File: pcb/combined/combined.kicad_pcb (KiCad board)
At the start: 2 copper layers, 113.5 x 87.5 mm, 67 parts, among them J1 5V POWER, J10 PRESSURE, J11 XIAO D0-D6, J12 XIAO D7-5V, J2 MAINS_IN, J3 VALVE, J4 PUMP, J5 CAN BUS, J6 FLOW HALL, J8 BOILER SSR, Q1 SS8050, Q2 BT136S, Q3 SS8050, Q4 BT136S, Q5 AO3401A, Q6 2N7002, U1 MOC3043M, U2 MOC3023M, U3 EL817C, U4 TJA1051T/3, U5 TMP102AIDRLR, U6 ADS1115IDGSR

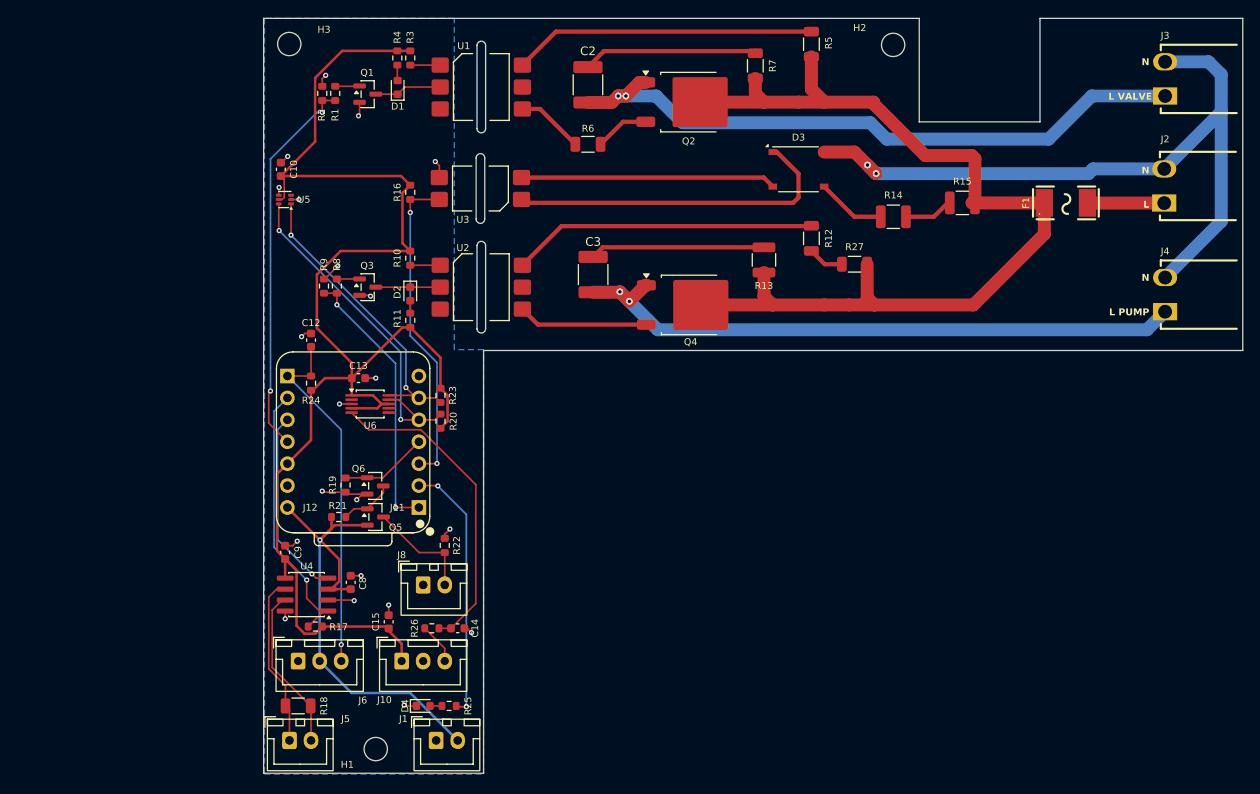
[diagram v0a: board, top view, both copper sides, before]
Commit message: Draw the combined v2 schematic: 24 V buck and isolated gear pump interface
The pump dimmer and the zero-cross detector leave the board; the 230 V
valve channel stays. J7 brings 24 V from the pump supply to an
LMR33630A buck (5.02 V, enable at 18.4 V, off at 16.9 V), and J1 now sends
5 V to the screen. Two EL817C keep the pump's signal wires on their
isolated side: U8 turns the 1 kHz PWM on GPIO1 into a filtered setpoint
from the pump's own 5 V, U9 brings the tachometer back to GPIO3. DIM and
ZC become PUMP_SPEED and PUMP_TACHO.

The XIAO 5V pin is its USB VBUS with no diode; no diode is added either,
so USB is never plugged in with the XIAO on the board. New parts take new
references, so that no low-voltage net inherits a stale Mains netclass
pattern; those patterns and the pump and zero-cross DRC rules are gone.

F1 drops to 0.5 A, now that it protects the valve alone, and the AC
tracks to 1 mm. J3 is reversed so that its N faces N on J2. The HT396R
outline follows the Kefa drawing, and J8 becomes an HT396V header whose
screw plug takes the 0.75 mm² wires to the boiler SSR.

The board has been updated from the schematic; placement and routing are
still in progress.

Co-Authored-By: Claude Opus 5.5 <noreply@anthropic.com>
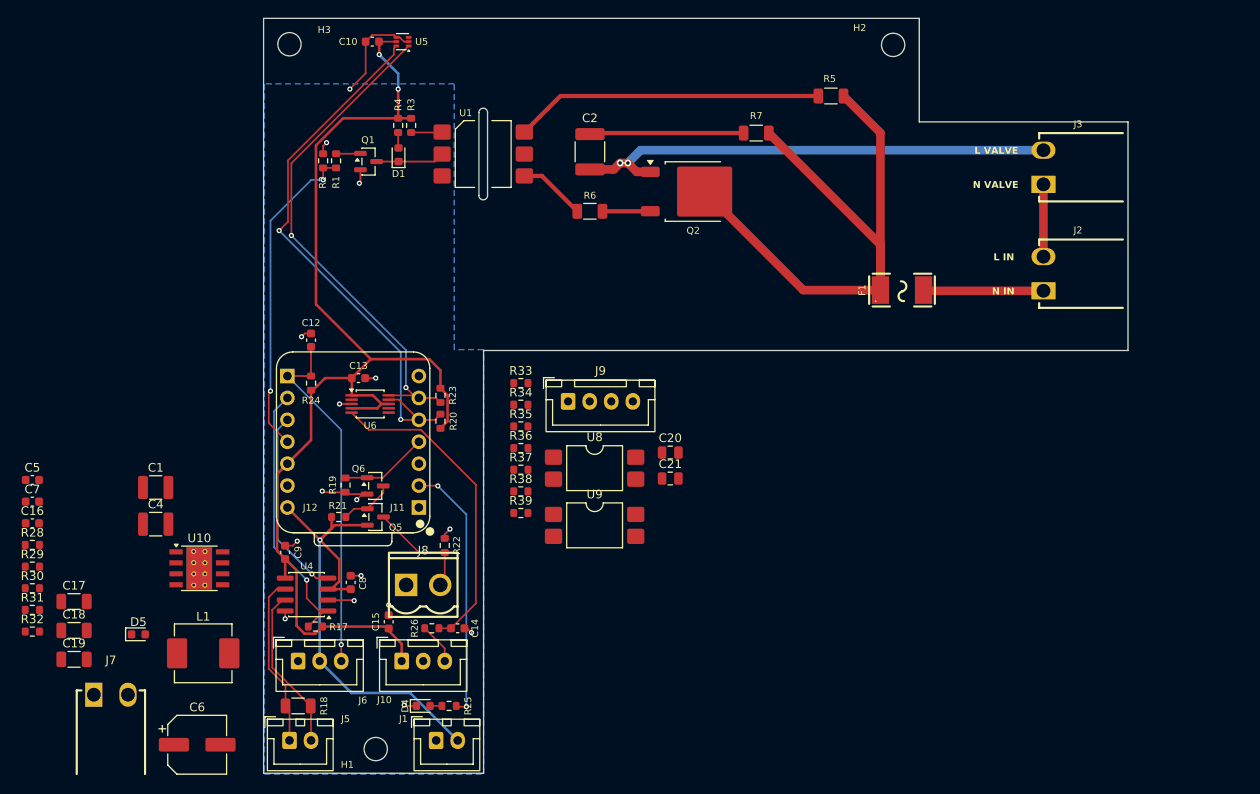
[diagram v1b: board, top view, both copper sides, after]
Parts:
- removed C3: 10nF 1kV, Capacitor_SMD:C_1812_4532Metric
- removed D2: RED, LED_SMD:LED_0603_1608Metric
- removed D3: ABS6, Diode_SMD:Diode_Bridge_Diotec_ABS
- removed J4: PUMP, Combined_Local:CONN-TH_P3.96_HT396R-3.96-2P
- removed Q3: SS8050, Package_TO_SOT_SMD:SOT-23
- removed Q4: BT136S, Package_TO_SOT_SMD:TO-252-2
- removed R10: 180, Resistor_SMD:R_0603_1608Metric
- removed R11, R8: 1k, Resistor_SMD:R_0603_1608Metric
- removed R12, R27: 510, Resistor_SMD:R_1206_3216Metric
- removed R13: 39, Resistor_SMD:R_1210_3225Metric
- removed R14, R15: 120k, Resistor_SMD:R_1210_3225Metric
- removed R16: 10k, Resistor_SMD:R_0603_1608Metric
- removed R9: 4.7k, Resistor_SMD:R_0603_1608Metric
- removed U2: MOC3023M, Combined_Local:SMDIP-6_W9.53mm_Slot
- removed U3: EL817C, Combined_Local:SMDIP-4_W9.53mm_Slot
- added C1: 10uF 50V, Capacitor_SMD:C_1210_3225Metric, F.Cu at (68.0, 101.4)
- added C16: 1uF, Capacitor_SMD:C_0603_1608Metric, F.Cu at (53.7, 105.5)
- added C17: 22uF, Capacitor_SMD:C_1206_3216Metric, F.Cu at (58.5, 114.6)
- added C18: 22uF, Capacitor_SMD:C_1206_3216Metric, F.Cu at (58.5, 118.0)
- added C19: 22uF, Capacitor_SMD:C_1206_3216Metric, F.Cu at (58.5, 121.3)
- added C20: 1.5uF, Capacitor_SMD:C_0805_2012Metric, F.Cu at (127.6, 97.3)
- added C21: 1.5uF, Capacitor_SMD:C_0805_2012Metric, F.Cu at (127.6, 100.3)
- added C4: 10uF 50V, Capacitor_SMD:C_1210_3225Metric, F.Cu at (68.0, 105.6)
- added C5: 100nF, Capacitor_SMD:C_0603_1608Metric, F.Cu at (53.7, 100.5)
- added C6: 47uF 50V, Capacitor_SMD:CP_Elec_6.3x7.7, F.Cu at (72.8, 131.2)
- added C7: 100nF, Capacitor_SMD:C_0603_1608Metric, F.Cu at (53.7, 103.0)
- added D5: 5V, LED_SMD:LED_0603_1608Metric, F.Cu at (66.0, 118.4)
- added J7: 24V IN, Combined_Local:CONN-TH_P3.96_HT396R-3.96-2P, F.Cu at (62.8, 125.4)
- added J9: PUMP, Connector_JST:JST_XH_B4B-XH-A_1x04_P2.50mm_Vertical, F.Cu at (115.8, 91.4)
- added L1: 10uH, Inductor_SMD:L_Changjiang_FXL0630, F.Cu at (73.5, 120.6)
- added R28: 100k, Resistor_SMD:R_0603_1608Metric, F.Cu at (53.7, 108.0)
- added R29: 24.9k, Resistor_SMD:R_0603_1608Metric, F.Cu at (53.7, 110.5)
- added R30: 100k, Resistor_SMD:R_0603_1608Metric, F.Cu at (53.7, 113.1)
- added R31: 7.15k, Resistor_SMD:R_0603_1608Metric, F.Cu at (53.7, 115.6)
- added R32: 1k, Resistor_SMD:R_0603_1608Metric, F.Cu at (53.7, 118.1)
- added R33: 330, Resistor_SMD:R_0603_1608Metric, F.Cu at (110.3, 89.3)
- added R34: 100k, Resistor_SMD:R_0603_1608Metric, F.Cu at (110.3, 91.8)
- added R35: 10k, Resistor_SMD:R_0603_1608Metric, F.Cu at (110.3, 94.3)
- added R36: 2.2k, Resistor_SMD:R_0603_1608Metric, F.Cu at (110.3, 96.8)
- added R37: 2.2k, Resistor_SMD:R_0603_1608Metric, F.Cu at (110.3, 99.3)
- added R38: 1.8k, Resistor_SMD:R_0603_1608Metric, F.Cu at (110.3, 101.8)
- added R39: 4.7k, Resistor_SMD:R_0603_1608Metric, F.Cu at (110.3, 104.3)
- added U10: LMR33630ADDAR, Package_SO:Texas_HSOP-8-1EP_3.9x4.9mm_P1.27mm_ThermalVias, F.Cu at (73.0, 110.8)
- added U8: EL817C, Package_DIP:SMDIP-4_W9.53mm, F.Cu at (118.9, 99.1)
- added U9: EL817C, Package_DIP:SMDIP-4_W9.53mm, F.Cu at (118.9, 105.8)
- F1: value 2A 250V fast -> 0.5A 250V fast
- J1: value 5V POWER -> 5V SCREEN
- J8: footprint Connector_JST:JST_XH_B2B-XH-A_1x02_P2.50mm_Vertical -> Combined_Local:CONN-TH_P3.96_HT396V-3.96-2P
- moved U5 22.8 mm to (96.6, 49.7)
- moved F1 21.5 mm to (154.5, 78.5)
- moved C10 18.2 mm to (93.1, 49.7), turned to 180 degrees
- moved J3 17.4 mm to (170.9, 64.3)
- moved J2 17.3 mm to (170.9, 76.6)
- moved Q2 10.4 mm to (130.4, 67.1)
- moved R1 7.81 mm to (88.9, 63.5)
- moved R2 7.81 mm to (87.4, 63.5)
- moved D1 7.81 mm to (96.1, 62.8)
- moved Q1 7.81 mm to (92.7, 63.6)
- moved R3 7.81 mm to (97.6, 59.4)
- moved R4 7.81 mm to (96.1, 59.4)
- moved R7 7.80 mm to (137.6, 60.3), turned to 180 degrees
- moved C2 7.77 mm to (118.3, 62.5)
- moved U1 7.77 mm to (106.0, 62.7)
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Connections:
- J11 pad 1: DIM -> PUMP_SPEED
- J11 pad 3: ZC -> PUMP_TACHO
- J3 pad 1: /L_VALVE -> /N
- J3 pad 2: /N -> /L_VALVE
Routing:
- net /N: track 84.8 -> 8.38 mm, vias 2 -> 0
- net /L_PUMP: track 73.3 -> 0.00 mm, vias 2 -> 0
- net /L: track 113.3 -> 72.7 mm
- net Net-(D3-+): track 40.0 -> 0.00 mm
- net ZC: track 37.4 -> 0.00 mm, vias 2 -> 0
- net Net-(R12-Pad1): track 35.4 -> 0.00 mm
- net DIM: track 31.9 -> 0.00 mm, vias 2 -> 0
- net +3V3: track 165.1 -> 134.4 mm, vias 0 -> 2
- net Net-(D3--): track 29.6 -> 0.00 mm
- net I2C_SCL: track 35.2 -> 59.1 mm
- net I2C_SDA: track 40.2 -> 64.1 mm
- net Net-(C3-Pad1): track 20.3 -> 0.00 mm
- net /L_VALVE: track 75.2 -> 56.5 mm
- net Net-(Q4-G): track 15.1 -> 0.00 mm
- net Net-(D3-Pad3): track 8.01 -> 0.00 mm
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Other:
- board size 113.5 x 87.5 mm -> 100.2 x 87.5 mm
- board text added: "L IN"
- board text added: "N IN"
- board text added: "N VALVE"
- board text removed: "L"
- board text removed: "L PUMP"
- board text removed: "N"

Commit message: Route combined v2: buck layout, POWER class with GND, GPIO table on the back
Shrink F.Fab texts to 0.5 mm and silkscreen texts to 0.8 mm. Put GND in
the POWER net class and enforce its 0.3 mm minimum by a DRC rule, with a
0.2 mm neck-down allowed at the TMP102. Add the XIAO GPIO table on
B.SilkS and the 24 V and 230 V ratings.

Swap R5 to C163378 and U6 to ADS1115IDGST (C468683), same parts in stock.
Fix the JLCPCB placement of U5 (+270) and J9 (pin-row midpoint, +180).

Co-Authored-By: Claude Opus 5.5 <noreply@anthropic.com>
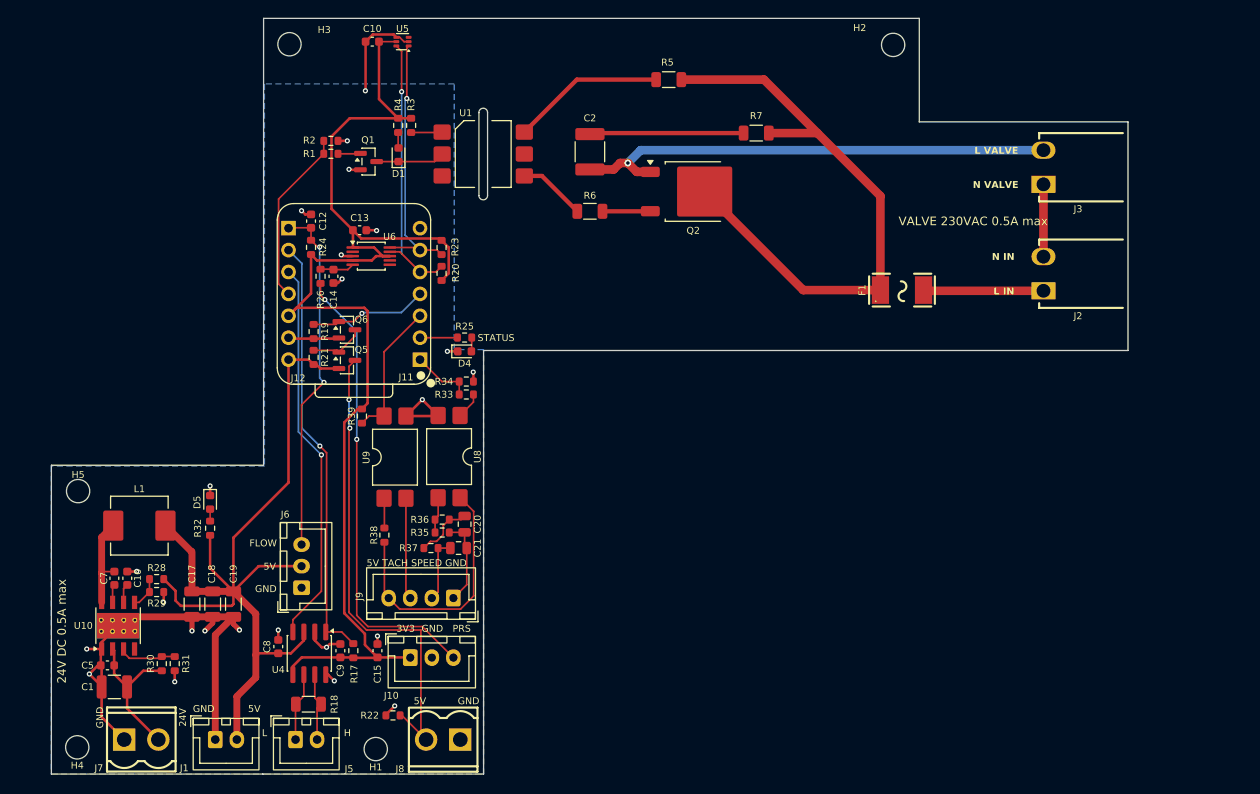
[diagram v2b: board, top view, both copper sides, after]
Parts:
- removed C4: 10uF 50V, Capacitor_SMD:C_1210_3225Metric
- removed C6: 47uF 50V, Capacitor_SMD:CP_Elec_6.3x7.7
- added H4: M2.5, MountingHole:MountingHole_2.7mm_M2.5, F.Cu at (58.9, 131.5)
- added H5: M2.5, MountingHole:MountingHole_2.7mm_M2.5, F.Cu at (59.0, 101.8)
- C5: value 100nF -> 220nF
- J7: footprint Combined_Local:CONN-TH_P3.96_HT396R-3.96-2P -> Combined_Local:CONN-TH_P3.96_HT396V-3.96-2P
- U6: value ADS1115IDGSR -> ADS1115IDGST
- moved C14 43.3 mm to (88.6, 76.9), turned to -90 degrees
- moved R26 42.8 mm to (87.1, 76.9), turned to 90 degrees
- moved R25 42.7 mm to (103.8, 84.0), turned to 0 degrees
- moved D4 41.4 mm to (103.8, 85.6)
- moved J9 26.4 mm to (102.5, 114.2), turned to 180 degrees
- moved C21 25.8 mm to (103.1, 108.4)
- moved J1 25.6 mm to (74.9, 130.6)
- moved C20 25.2 mm to (103.8, 105.6), turned to -90 degrees
- moved U9 24.5 mm to (95.7, 97.9), turned to 90 degrees
- moved R32 23.8 mm to (74.3, 106.1), turned to 90 degrees
- moved C1 23.6 mm to (63.2, 124.5), turned to 180 degrees
- moved C5 23.2 mm to (62.4, 122.0), turned to 180 degrees
- moved R39 21.6 mm to (91.9, 93.1), turned to -90 degrees
- moved R22 20.6 mm to (95.5, 127.8), turned to 180 degrees
- moved C19 19.6 mm to (77.0, 114.9), turned to -90 degrees
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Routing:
- net GND: track 37.7 -> 105.2 mm, vias 16 -> 24
- net PRESSURE: track 4.76 -> 53.4 mm, vias 0 -> 2
- net +5V: track 60.2 -> 104.2 mm, vias 1 -> 0
- net /Interfaces/BOILER_5V: track 12.6 -> 55.9 mm, vias 0 -> 2
- net PRESSURE_ADC: track 37.1 -> 3.98 mm
- net /+5V_P: track 0.00 -> 29.7 mm
- net I2C_SDA: track 64.1 -> 34.6 mm, vias 2 -> 1
- net I2C_SCL: track 59.1 -> 30.9 mm, vias 2 -> 1
- net /Controller/STATUS_LED: track 30.4 -> 4.35 mm, vias 2 -> 0
- net CAN_RX: track 22.0 -> 44.7 mm
- net CAN_TX: track 31.5 -> 49.9 mm
- net Net-(R5-Pad1): track 36.0 -> 17.8 mm
- net +24V: track 0.00 -> 17.5 mm
- net SSR: track 37.5 -> 20.4 mm, vias 2 -> 0
- net PUMP_TACHO: track 0.00 -> 16.2 mm
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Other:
- board size 100.2 x 87.5 mm -> 124.8 x 87.6 mm
- board text added: "-"
- board text added: "1"
- board text added: "2"
- board text added: "24V"
- board text added: "24V DC 0.5A max"
- board text added: "3"
- board text added: "3V3"
- board text added: "4"
- board text added: "43"
- board text added: "44"
- board text added: "5"
- board text added: "5V"
- board text added: "5V TACH SPEED GND"
- board text added: "6"
- board text added: "7"
- board text added: "8"
- board text added: "9"
- board text added: "BOILER SSR"
- board text added: "CAN RX"
- board text added: "CAN TX"
- board text added: "D0"
- board text added: "D1"
- board text added: "D10"
- board text added: "D2"
- board text added: "D3"
- board text added: "D4"
- board text added: "D5"
- board text added: "D6"
- board text added: "D7"
- board text added: "D8"
- board text added: "D9"
- board text added: "FLOW"
- board text added: "FLOW HALL"
- board text added: "FREE"
- board text added: "FUNCTION"
- board text added: "GEAR PUMP PWM"
- board text added: "GEAR PUMP TACHO"
- board text added: "GND"
- board text added: "GPIO"
- board text added: "H"
- board text added: "I2C SCL"
- board text added: "I2C SDA"
- board text added: "J3"
- board text added: "J5"
- board text added: "J6"
- board text added: "J8"
- board text added: "J9"
- board text added: "L"
- board text added: "PAD"
- board text added: "PART"
- board text added: "PRS"
- board text added: "STATUS"
- board text added: "STATUS LED"
- board text added: "U5 U6"
- board text added: "VALVE"
- board text added: "VALVE 230VAC 0.5A max"
- board text added: "XIAO ESP32-S3"

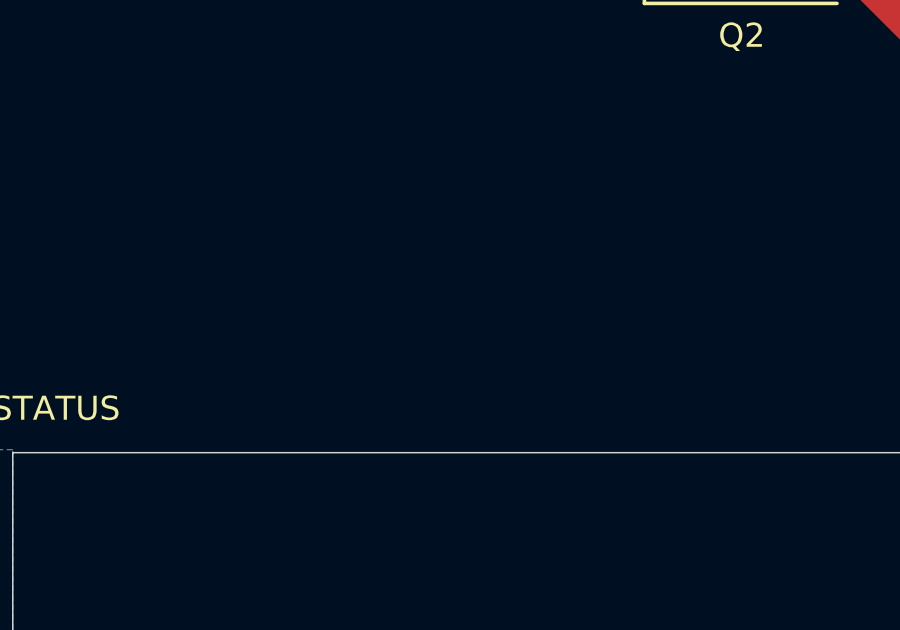
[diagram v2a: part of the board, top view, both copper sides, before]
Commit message: Add H6 on the combined mains side and drop the nylon hardware
H6, a sixth M2.5 mounting hole, sits low in the 230 VAC area. From the
edge of the hardware (2.9 mm radius, a 5 mm hex standoff), H2 is 8.8 mm
from the mains copper and H6 9.6 mm from it and 12.5 mm from the GND
plane: each gap clears the 7 mm reinforced distance alone, so both take
metal screws and standoffs into the floating brass inserts. H1, H4 and
H5 have only GND plane under their hardware and need no keepout.

Co-Authored-By: Claude Opus 5.5 <noreply@anthropic.com>
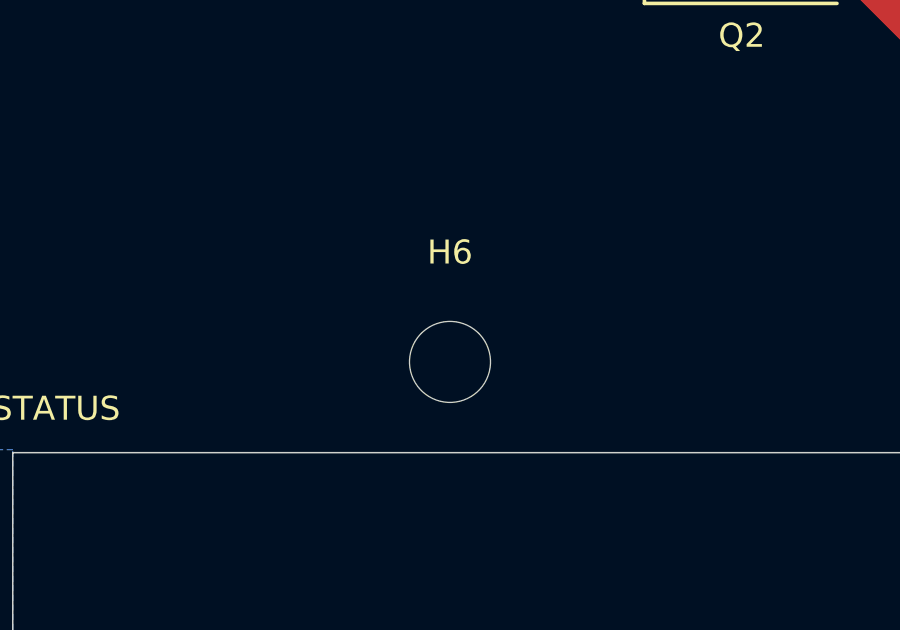
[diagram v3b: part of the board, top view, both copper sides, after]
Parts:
- added H6: M2.5, MountingHole:MountingHole_2.7mm_M2.5, F.Cu at (120.6, 82.5)
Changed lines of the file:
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@@
 		)
+	)
+	(footprint "MountingHole:MountingHole_2.7mm_M2.5"
+		(layer "F.Cu")
+		(at 120.575 82.475)
+		(descr "Mounting Hole 2.7mm, M2.5, no annular, generated by kicad-footprint-generator mountinghole.py")
+		(tags "mountinghole M2.5")
+		(property "Reference" "H6"
+			(at 0 -3.65 0)
+			(layer "F.SilkS")
+			(effects
+				(font
+					(size 0.8 0.8)
+					(thickness 0.15)
+				)
+			)
+		)
+		(property "Value" "M2.5"
+			(at 0 3.65 0)
+			(layer "F.Fab")
+			(effects
+				(font
+					(size 1 1)
+					(thickness 0.15)
+				)
+			)
+		)
+		(property "Datasheet" ""
+			(at 0 0 0)
+			(layer "F.Fab")
+			(hide yes)
+			(effects
+				(font
+					(size 1.27 1.27)
+				)
+			)
+		)
+		(property "Description" "Mounting Hole without connection"
+			(at 0 0 0)
+			(layer "F.Fab")
+			(hide yes)
+			(effects
+				(font
+					(size 1.27 1.27)
+				)
+			)
+		)
+		(property "MPN" "M2.5 / 2.7mm"
+			(at 0 0 0)
+			(unlocked yes)
+			(layer "F.Fab")
+			(hide yes)
+			(effects
+				(font
+					(size 1 1)
+					(thickness 0.15)
+				)
+			)
+		)
+		(property ki_fp_filters "MountingHole*")
+		(sheetname "/Controller/")
+		(sheetfile "combined_controller.kicad_sch")
+		(units
+			(unit
+				(name "A")
+				(pins)
+			)
+		)
+		(attr exclude_from_bom)
+		(duplicate_pad_numbers_are_jumpers no)
+		(fp_circle
+			(center 0 0)
+			(end 2.7 0)
+			(stroke
+				(width 0.15)
+				(type solid)
+			)
+			(fill no)
+			(layer "Cmts.User")
+		)
+		(fp_circle
+			(center 0 0)
+			(end 2.95 0)
+			(stroke
+				(width 0.05)
+				(type solid)
+			)
+			(fill no)
+			(layer "F.CrtYd")
+		)
+		(fp_text user "${REFERENCE}"
+			(at 0 0 0)
+			(layer "F.Fab")
+			(effects
+				(font
+					(size 1 1)
+					(thickness 0.15)
+				)
+			)
+		)
+		(pad "" np_thru_hole circle
+			(at 0 0)
+			(size 2.7 2.7)
+			(drill 2.7)
+			(layers "*.Cu" "*.Mask")
+		)
+		(embedded_fonts no)
 	)
 	(footprint "Package_SO:Texas_HSOP-8-1EP_3.9x4.9mm_P1.27mm_ThermalVias"
